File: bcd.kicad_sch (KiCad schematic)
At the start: 1 part

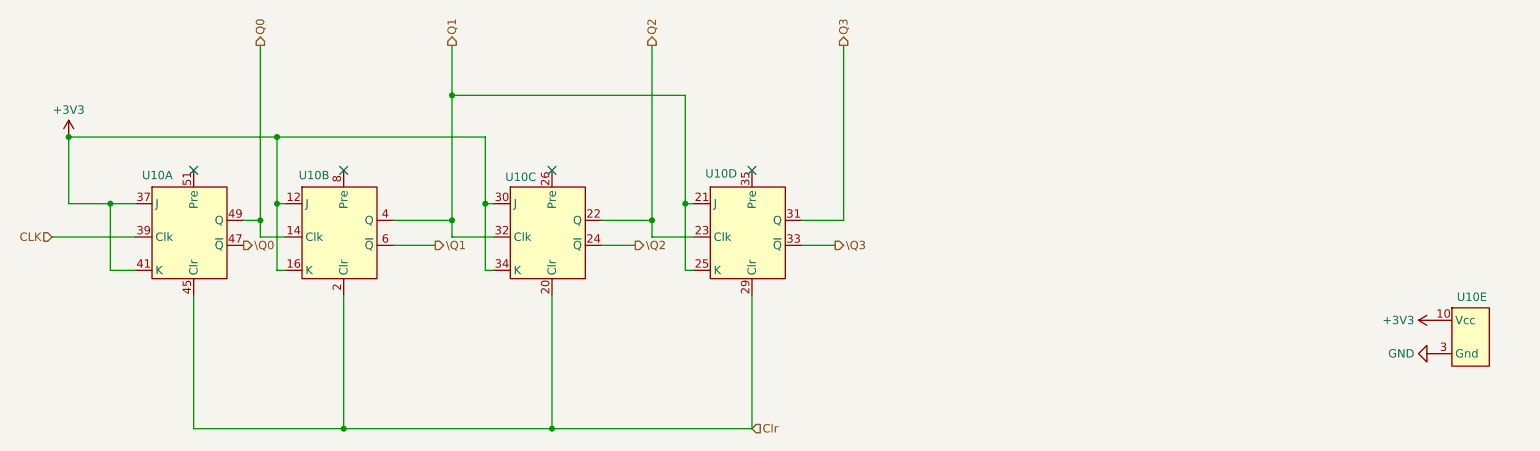
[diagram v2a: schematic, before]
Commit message: added module for PSU
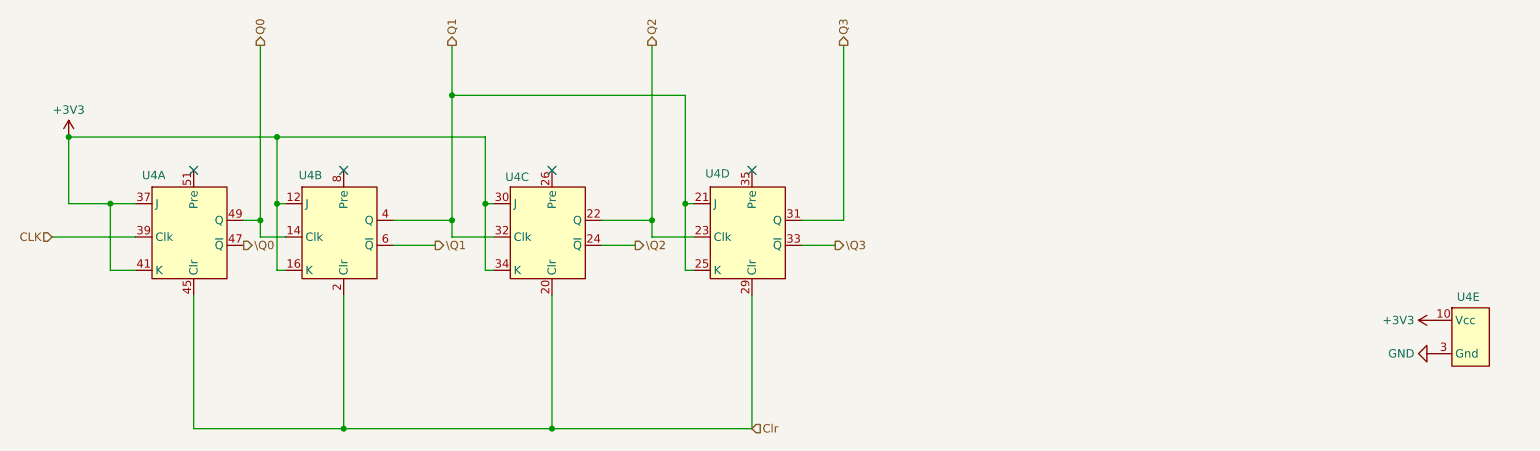
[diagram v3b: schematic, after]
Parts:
- U4: renamed from U10; value ~ -> flipflop; LCSC Part # (none) -> C185937
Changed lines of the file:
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@@
 		(on_board yes)
 		(dnp no)
-		(property "Reference" "U10"
+		(property "Reference" "U4"
 			(at 122.428 105.156 0)
 			(effects
@@
 			)
 		)
-		(property "Value" "~"
+		(property "Value" "flipflop"
 			(at 139.3033 107.6268 0)
 			(effects
@@
 			)
 		)
-		(property "LCSC Part #" ""
+		(property "LCSC Part #" "C185937"
 			(at 124.46 105.41 0)
 			(effects
@@
 			(project "transistor-clock"
 				(path "/ce10d5bc-995e-4952-aa76-0a08f713a0f2/2c36a9e9-de42-4705-9ad4-94f4cc168e2f/213ead95-e2da-4b6f-a756-d929eb6dfb1c"
-					(reference "U16")
-					(unit 3)
-				)
-				(path "/ce10d5bc-995e-4952-aa76-0a08f713a0f2/2c36a9e9-de42-4705-9ad4-94f4cc168e2f/230aee3b-3cdc-400c-8fed-9199df89dadd"
 					(reference "U10")
 					(unit 3)
 				)
+				(path "/ce10d5bc-995e-4952-aa76-0a08f713a0f2/2c36a9e9-de42-4705-9ad4-94f4cc168e2f/230aee3b-3cdc-400c-8fed-9199df89dadd"
+					(reference "U4")
+					(unit 3)
+				)
 				(path "/ce10d5bc-995e-4952-aa76-0a08f713a0f2/2c36a9e9-de42-4705-9ad4-94f4cc168e2f/6fa12e35-b957-4335-be8e-d0857c2dd0bf"
-					(reference "U13")
+					(reference "U7")
 					(unit 3)
 				)
@@
 		(on_board yes)
 		(dnp no)
-		(property "Reference" "U10"
+		(property "Reference" "U4"
 			(at 267.462 123.444 0)
 			(effects
@@
 			)
 		)
-		(property "Value" "~"
+		(property "Value" "flipflop"
 			(at 276.4633 122.8668 0)
 			(effects
@@
 			)
 		)
-		(property "LCSC Part #" ""
+		(property "LCSC Part #" "C185937"
 			(at 261.62 120.65 0)
 			(effects
@@
 			(project "transistor-clock"
 				(path "/ce10d5bc-995e-4952-aa76-0a08f713a0f2/2c36a9e9-de42-4705-9ad4-94f4cc168e2f/213ead95-e2da-4b6f-a756-d929eb6dfb1c"
-					(reference "U16")
-					(unit 5)
-				)
-				(path "/ce10d5bc-995e-4952-aa76-0a08f713a0f2/2c36a9e9-de42-4705-9ad4-94f4cc168e2f/230aee3b-3cdc-400c-8fed-9199df89dadd"
 					(reference "U10")
 					(unit 5)
 				)
+				(path "/ce10d5bc-995e-4952-aa76-0a08f713a0f2/2c36a9e9-de42-4705-9ad4-94f4cc168e2f/230aee3b-3cdc-400c-8fed-9199df89dadd"
+					(reference "U4")
+					(unit 5)
+				)
 				(path "/ce10d5bc-995e-4952-aa76-0a08f713a0f2/2c36a9e9-de42-4705-9ad4-94f4cc168e2f/6fa12e35-b957-4335-be8e-d0857c2dd0bf"
-					(reference "U13")
+					(reference "U7")
 					(unit 5)
 				)
@@
 		(on_board yes)
 		(dnp no)
-		(property "Reference" "U10"
+		(property "Reference" "U4"
 			(at 152.908 104.648 0)
 			(effects
@@
 			)
 		)
-		(property "Value" "~"
+		(property "Value" "flipflop"
 			(at 169.7833 106.3568 0)
 			(effects
@@
 			)
 		)
-		(property "LCSC Part #" ""
+		(property "LCSC Part #" "C185937"
 			(at 154.94 105.41 0)
 			(effects
@@
 			(project "transistor-clock"
 				(path "/ce10d5bc-995e-4952-aa76-0a08f713a0f2/2c36a9e9-de42-4705-9ad4-94f4cc168e2f/213ead95-e2da-4b6f-a756-d929eb6dfb1c"
-					(reference "U16")
-					(unit 4)
-				)
-				(path "/ce10d5bc-995e-4952-aa76-0a08f713a0f2/2c36a9e9-de42-4705-9ad4-94f4cc168e2f/230aee3b-3cdc-400c-8fed-9199df89dadd"
 					(reference "U10")
 					(unit 4)
 				)
+				(path "/ce10d5bc-995e-4952-aa76-0a08f713a0f2/2c36a9e9-de42-4705-9ad4-94f4cc168e2f/230aee3b-3cdc-400c-8fed-9199df89dadd"
+					(reference "U4")
+					(unit 4)
+				)
 				(path "/ce10d5bc-995e-4952-aa76-0a08f713a0f2/2c36a9e9-de42-4705-9ad4-94f4cc168e2f/6fa12e35-b957-4335-be8e-d0857c2dd0bf"
-					(reference "U13")
+					(reference "U7")
 					(unit 4)
 				)
@@
 		(on_board yes)
 		(dnp no)
-		(property "Reference" "U10"
+		(property "Reference" "U4"
 			(at 67.056 104.902 0)
 			(effects
@@
 			)
 		)
-		(property "Value" "~"
+		(property "Value" "flipflop"
 			(at 84.455 111.3846 0)
 			(effects
@@
 			)
 		)
-		(property "LCSC Part #" ""
+		(property "LCSC Part #" "C185937"
 			(at 69.85 105.41 0)
 			(effects
@@
 			(project "transistor-clock"
 				(path "/ce10d5bc-995e-4952-aa76-0a08f713a0f2/2c36a9e9-de42-4705-9ad4-94f4cc168e2f/213ead95-e2da-4b6f-a756-d929eb6dfb1c"
-					(reference "U16")
+					(reference "U10")
 					(unit 1)
 				)
 				(path "/ce10d5bc-995e-4952-aa76-0a08f713a0f2/2c36a9e9-de42-4705-9ad4-94f4cc168e2f/230aee3b-3cdc-400c-8fed-9199df89dadd"
-					(reference "U10")
+					(reference "U4")
 					(unit 1)
 				)
 				(path "/ce10d5bc-995e-4952-aa76-0a08f713a0f2/2c36a9e9-de42-4705-9ad4-94f4cc168e2f/6fa12e35-b957-4335-be8e-d0857c2dd0bf"
-					(reference "U13")
+					(reference "U7")
 					(unit 1)
 				)
@@
 		(on_board yes)
 		(dnp no)
-		(property "Reference" "U10"
+		(property "Reference" "U4"
 			(at 90.932 104.902 0)
 			(effects
@@
 			)
 		)
-		(property "Value" "~"
+		(property "Value" "flipflop"
 			(at 105.0133 105.0868 0)
 			(effects
@@
 			)
 		)
-		(property "LCSC Part #" ""
+		(property "LCSC Part #" "C185937"
 			(at 92.71 105.41 0)
 			(effects
@@
 			(project "transistor-clock"
 				(path "/ce10d5bc-995e-4952-aa76-0a08f713a0f2/2c36a9e9-de42-4705-9ad4-94f4cc168e2f/213ead95-e2da-4b6f-a756-d929eb6dfb1c"
-					(reference "U16")
-					(unit 2)
-				)
-				(path "/ce10d5bc-995e-4952-aa76-0a08f713a0f2/2c36a9e9-de42-4705-9ad4-94f4cc168e2f/230aee3b-3cdc-400c-8fed-9199df89dadd"
 					(reference "U10")
 					(unit 2)
 				)
+				(path "/ce10d5bc-995e-4952-aa76-0a08f713a0f2/2c36a9e9-de42-4705-9ad4-94f4cc168e2f/230aee3b-3cdc-400c-8fed-9199df89dadd"
+					(reference "U4")
+					(unit 2)
+				)
 				(path "/ce10d5bc-995e-4952-aa76-0a08f713a0f2/2c36a9e9-de42-4705-9ad4-94f4cc168e2f/6fa12e35-b957-4335-be8e-d0857c2dd0bf"
-					(reference "U13")
+					(reference "U7")
 					(unit 2)
 				)

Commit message: flipflop sims
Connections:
- net +3V3: now also U4.26 (Pre), U4.35 (Pre), U4.51 (Pre), U4.8 (Pre)
- no-connect marks 4 -> 0
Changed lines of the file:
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@@
 	(paper "A4")
 	(junction
+		(at 119.38 99.06)
+		(diameter 0)
+		(color 0 0 0 0)
+	)
+	(junction
 		(at 55.88 99.06)
 		(diameter 0)
@@
 	)
 	(junction
+		(at 97.79 99.06)
+		(diameter 0)
+		(color 0 0 0 0)
+	)
+	(junction
 		(at 129.54 143.51)
 		(diameter 0)
@@
 	)
 	(junction
+		(at 129.54 99.06)
+		(diameter 0)
+		(color 0 0 0 0)
+	)
+	(junction
+		(at 74.93 99.06)
+		(diameter 0)
+		(color 0 0 0 0)
+	)
+	(junction
 		(at 114.3 111.76)
 		(diameter 0)
@@
 		(color 0 0 0 0)
 	)
-	(no_connect
-		(at 129.54 104.14)
-	)
-	(no_connect
-		(at 160.02 104.14)
-	)
-	(no_connect
-		(at 74.93 104.14)
-	)
-	(no_connect
-		(at 97.79 104.14)
-	)
-	(wire
-		(pts
-			(xy 55.88 99.06) (xy 87.63 99.06)
+	(wire
+		(pts
+			(xy 55.88 99.06) (xy 74.93 99.06)
 		)
 		(stroke
@@
 	(wire
 		(pts
+			(xy 97.79 99.06) (xy 119.38 99.06)
+		)
+		(stroke
+			(width 0)
+			(type default)
+		)
+	)
+	(wire
+		(pts
 			(xy 62.23 119.38) (xy 66.04 119.38)
 		)
@@
 	(wire
 		(pts
+			(xy 129.54 99.06) (xy 160.02 99.06)
+		)
+		(stroke
+			(width 0)
+			(type default)
+		)
+	)
+	(wire
+		(pts
 			(xy 129.54 123.19) (xy 129.54 143.51)
 		)
@@
 	(wire
 		(pts
-			(xy 87.63 99.06) (xy 119.38 99.06)
+			(xy 87.63 99.06) (xy 97.79 99.06)
 		)
 		(stroke
@@
 	(wire
 		(pts
+			(xy 74.93 99.06) (xy 74.93 104.14)
+		)
+		(stroke
+			(width 0)
+			(type default)
+		)
+	)
+	(wire
+		(pts
 			(xy 74.93 143.51) (xy 97.79 143.51)
 		)
@@
 	(wire
 		(pts
+			(xy 119.38 99.06) (xy 129.54 99.06)
+		)
+		(stroke
+			(width 0)
+			(type default)
+		)
+	)
+	(wire
+		(pts
 			(xy 97.79 123.19) (xy 97.79 143.51)
 		)
@@
 	(wire
 		(pts
+			(xy 97.79 99.06) (xy 97.79 104.14)
+		)
+		(stroke
+			(width 0)
+			(type default)
+		)
+	)
+	(wire
+		(pts
 			(xy 88.9 109.22) (xy 87.63 109.22)
 		)
@@
 	(wire
 		(pts
+			(xy 129.54 104.14) (xy 129.54 99.06)
+		)
+		(stroke
+			(width 0)
+			(type default)
+		)
+	)
+	(wire
+		(pts
 			(xy 105.41 111.76) (xy 114.3 111.76)
 		)
@@
 	(wire
 		(pts
+			(xy 74.93 99.06) (xy 87.63 99.06)
+		)
+		(stroke
+			(width 0)
+			(type default)
+		)
+	)
+	(wire
+		(pts
 			(xy 66.04 109.22) (xy 62.23 109.22)
 		)
@@
 		)
 		(stroke
+			(width 0)
+			(type default)
+		)
+	)
+	(wire
+		(pts
+			(xy 160.02 104.14) (xy 160.02 99.06)
+		)
+		(stroke
